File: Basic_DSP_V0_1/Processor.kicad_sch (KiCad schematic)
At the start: 16 parts, among them J12 Conn_ARM_SWD_TagConnect_TC2030, U1 STM32F415RGTx

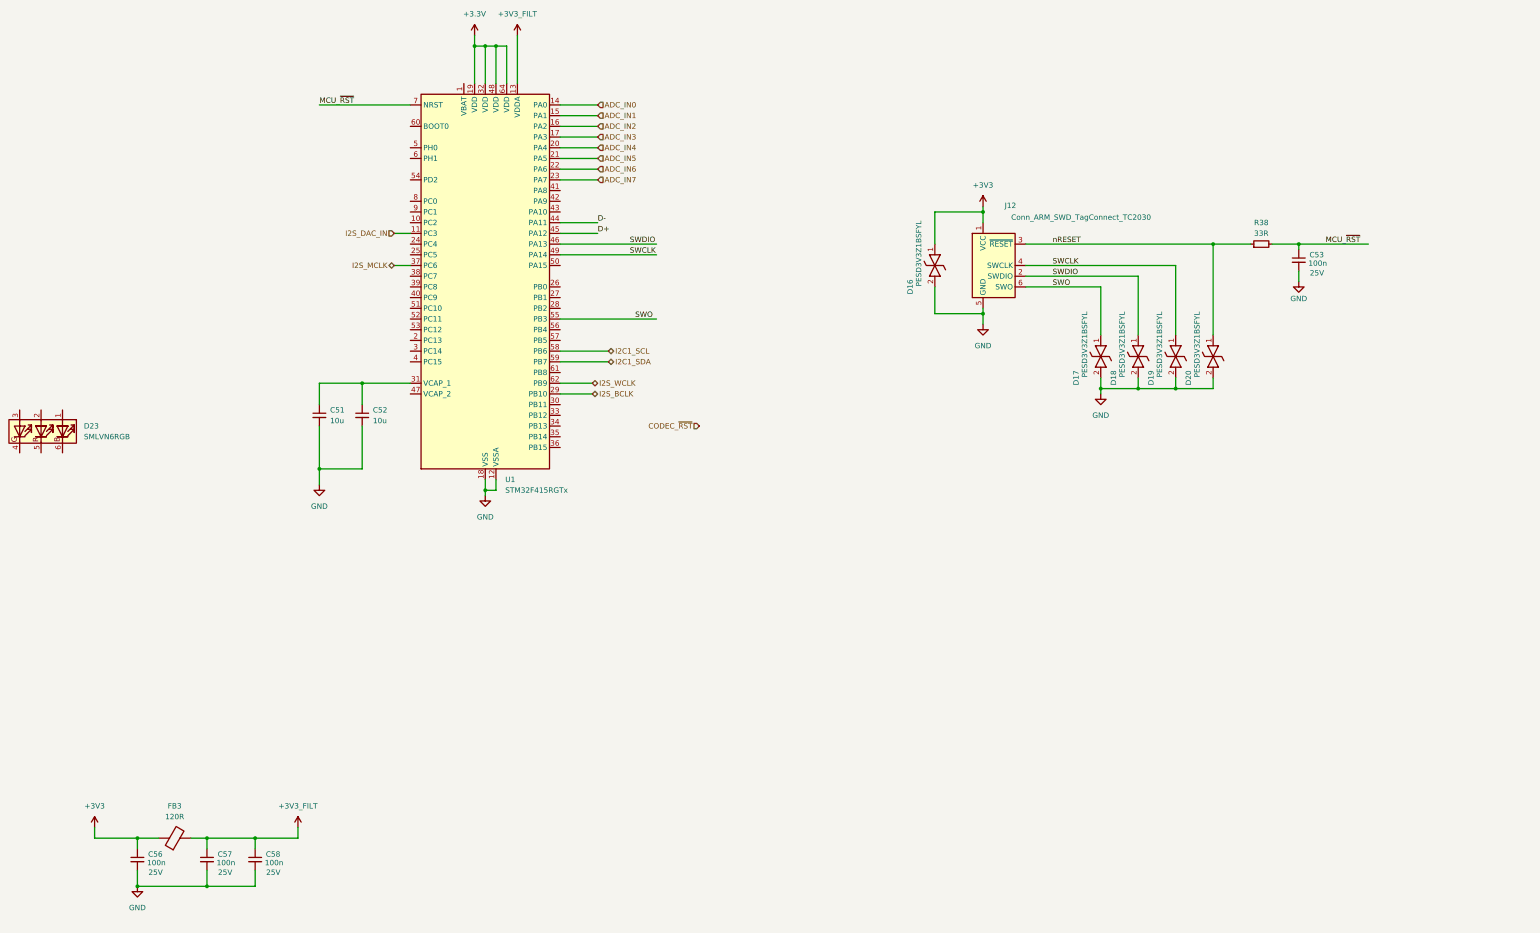
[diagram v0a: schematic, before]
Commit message: Updates to basic DSP schematic
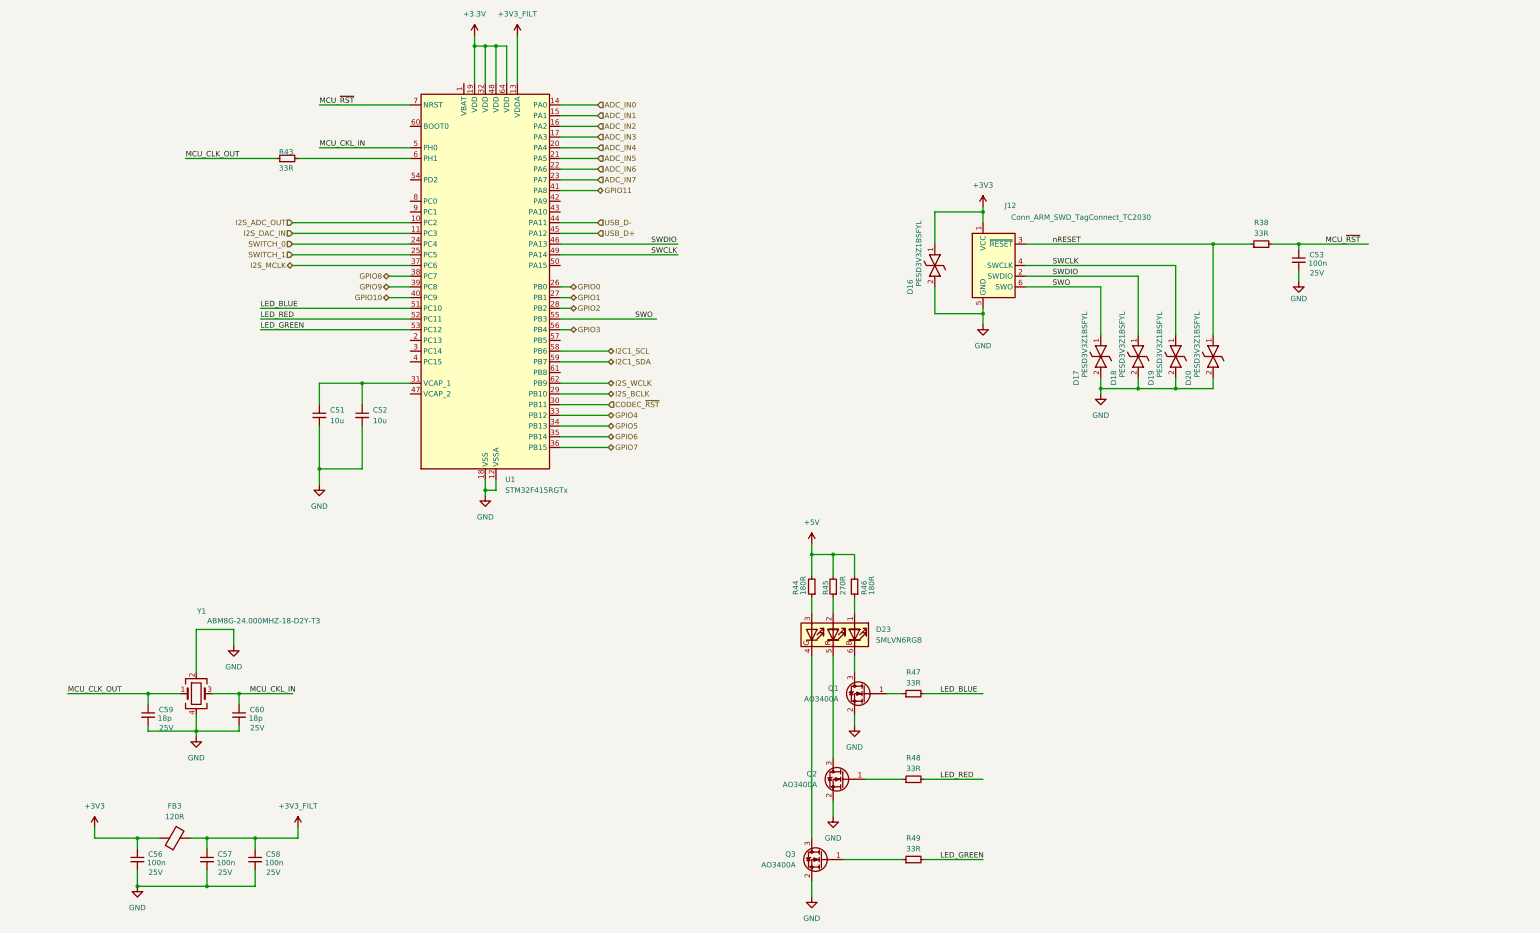
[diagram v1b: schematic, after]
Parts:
- added C59, C60: 18p, Capacitor_SMD:C_0402_1005Metric, symbol Device:C_Small
- added Q1, Q2, Q3: AO3400A, Package_TO_SOT_SMD:SOT-23, symbol Transistor_FET:AO3400A
- added R43, R47, R48, R49: 33R, Resistor_SMD:R_0402_1005Metric_Pad0.72x0.64mm_HandSolder, symbol Device:R_Small
- added R44, R46: 180R, Resistor_SMD:R_0402_1005Metric_Pad0.72x0.64mm_HandSolder, symbol Device:R_Small
- added R45: 270R, Resistor_SMD:R_0402_1005Metric_Pad0.72x0.64mm_HandSolder, symbol Device:R_Small
- added Y1: ABM8G-24.000MHZ-18-D2Y-T3, Crystal:Crystal_SMD_Abracon_ABM8G-4Pin_3.2x2.5mm, symbol Device:Crystal_GND24
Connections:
- net CODEC_~{RST}: now also U1.30 (PB11)
- net GND: now also C59.2, C60.2, Q1.2 (S), Q2.2 (S), Q3.2 (S), Y1.2, Y1.4
- net at D23.1 (BA): now also R46.1
- net at D23.2 (RA): now also R45.1
- net at D23.3 (GA): now also R44.1
- net at D23.4 (GK): now also Q3.3 (D)
- net at D23.5 (RK): now also Q2.3 (D)
- net at D23.6 (BK): now also Q1.3 (D)
- net I2S_ADC_OUT: now reaches U1.10 (PC2)
- net SWITCH_0: now reaches U1.24 (PC4)
- net SWITCH_1: now reaches U1.25 (PC5)
- net GPIO0: now reaches U1.26 (PB0)
- net GPIO1: now reaches U1.27 (PB1)
- net GPIO2: now reaches U1.28 (PB2)
- net GPIO4: now reaches U1.33 (PB12)
- net GPIO5: now reaches U1.34 (PB13)
- net GPIO6: now reaches U1.35 (PB14)
- net GPIO7: now reaches U1.36 (PB15)
- net GPIO8: now reaches U1.38 (PC7)
- net GPIO9: now reaches U1.39 (PC8)
- net GPIO10: now reaches U1.40 (PC9)
- net GPIO11: now reaches U1.41 (PA8)
- net MCU_CKL_IN: now reaches U1.5 (PH0)
- net MCU_CKL_IN: now also C60.1, Y1.3
- net LED_BLUE: now reaches U1.51 (PC10)
- net LED_BLUE: now also R47.2
- net LED_RED: now reaches U1.52 (PC11)
- net LED_RED: now also R48.2
- net LED_GREEN: now reaches U1.53 (PC12)
- net LED_GREEN: now also R49.2
- net GPIO3: now reaches U1.56 (PB4)
- net at U1.6 (PH1): now also R43.2
- net D+ renamed USB_D+
- net D- renamed USB_D-
- new net: Q1.1 (G), R47.1
- new net: Q2.1 (G), R48.1
- new net: Q3.1 (G), R49.1
- new net +5V: R44.2, R45.2, R46.2
- new net MCU_CLK_OUT: C59.1, R43.1, Y1.1
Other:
- moved on the sheet: D23

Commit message: Minor updates to Basic schematic
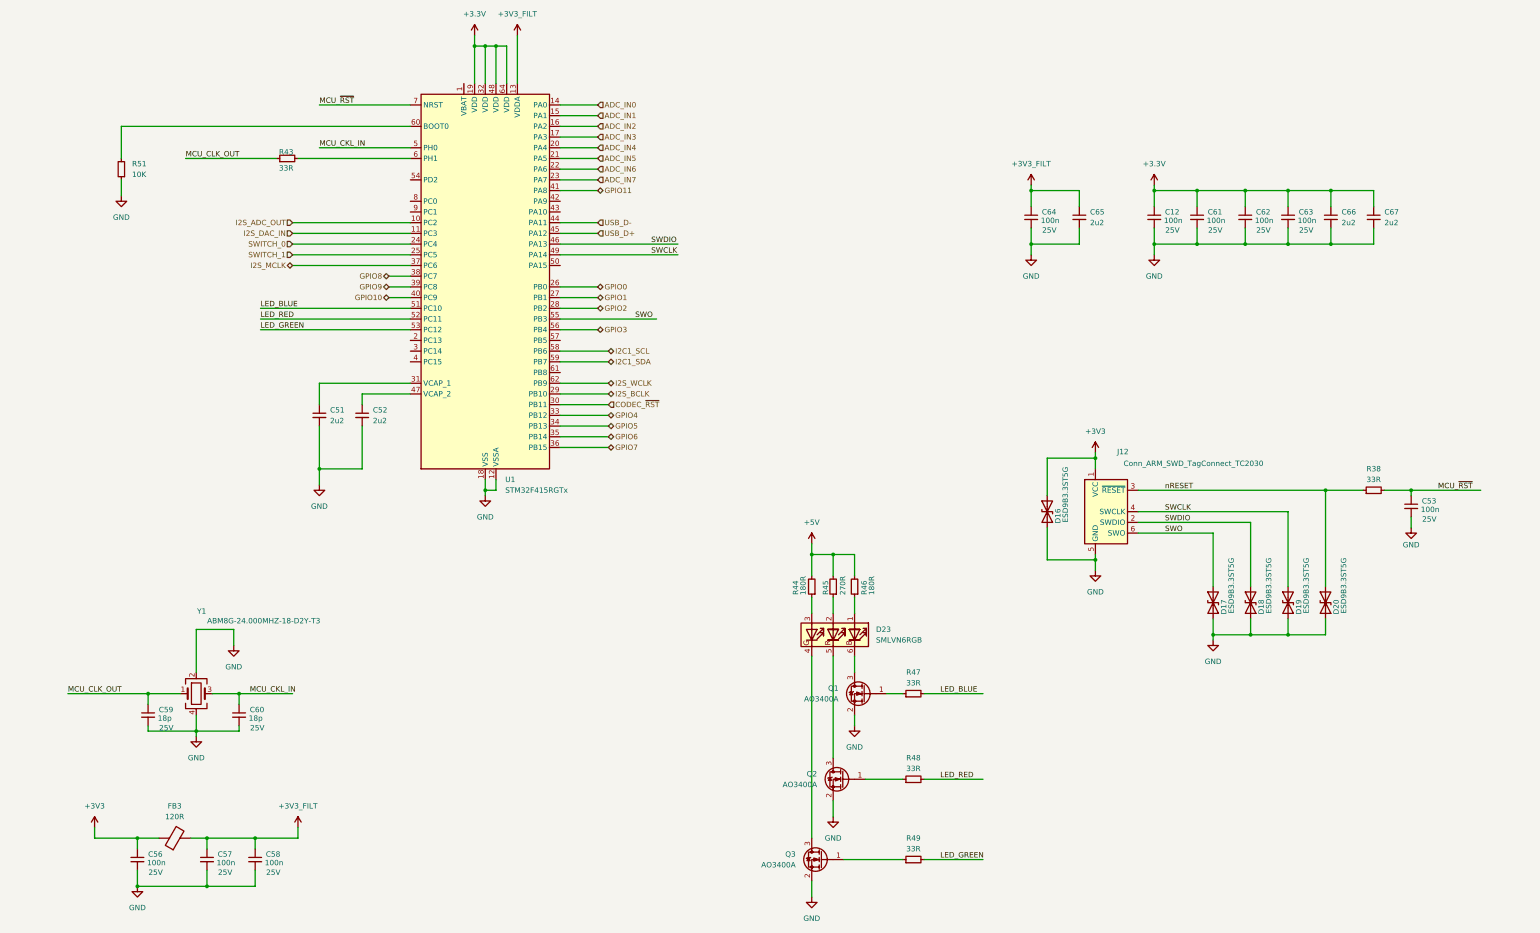
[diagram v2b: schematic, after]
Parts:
- removed D16, D17, D18, D19, D20: PESD3V3Z1BSFYL, symbol Chase_Diode:PESD3V3Z1BSFYL
- added C12: 100n, Capacitor_SMD:C_0603_1608Metric_Pad1.08x0.95mm_HandSolder, symbol Device:C_Small
- added C61, C62, C63, C64: 100n, Capacitor_SMD:C_0402_1005Metric, symbol Device:C_Small
- added C65, C66, C67: 2u2, Capacitor_SMD:C_0805_2012Metric, symbol Device:C_Small
- added D16, D17, D18, D19, D20: ESD9B3.3ST5G, Diode_SMD:D_SOD-923, symbol Diode:ESD9B3.3ST5G
- added R51: 10K, Resistor_SMD:R_0603_1608Metric_Pad0.98x0.95mm_HandSolder, symbol Device:R_Small
- C51, C52: value 10u -> 2u2; MPN CL21B106KOQNNNG -> (none); OC_MOUSER 187-CL21B106KOQNNNG -> (none)
- R38, R43, R44, R45, R46, R47, R48, R49: footprint Resistor_SMD:R_0402_1005Metric_Pad0.72x0.64mm_HandSolder -> Resistor_SMD:R_0603_1608Metric_Pad0.98x0.95mm_HandSolder
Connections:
- net +3.3V: now also C12.1, C61.1, C62.1, C63.1, C66.1, C67.1
- net +3V3: now also D16.2 (A2)
- net +3V3_FILT: now also C64.1, C65.1
- net GND: now also C12.2, C61.2, C62.2, C63.2, C64.2, C65.2, C66.2, C67.2, D16.1 (A1), D17.1 (A1), D18.1 (A1), D19.1 (A1), D20.1 (A1), R51.1
- net SWCLK: now also D19.2 (A2)
- net SWDIO: now also D18.2 (A2)
- net SWO: now also D17.2 (A2)
- net nRESET: now also D20.2 (A2)
- net at C51.1, U1.31 (VCAP_1): no longer C52.1
- net at U1.47 (VCAP_2): now also C52.1
- net at U1.60 (BOOT0): now also R51.2
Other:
- moved on the sheet: C53, J12, R38

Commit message: Started layout
Removed library from repo as it was messin with the links
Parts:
- C53, C56, C57, C58, C59, C60, C61, C62, C63, C64: footprint Capacitor_SMD:C_0402_1005Metric -> Capacitor_SMD:C_0603_1608Metric_Pad1.08x0.95mm_HandSolder
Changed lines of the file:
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@@
 			)
 		)
-		(property "Footprint" "Capacitor_SMD:C_0402_1005Metric"
+		(property "Footprint" "Capacitor_SMD:C_0603_1608Metric_Pad1.08x0.95mm_HandSolder"
 			(at 87.63 191.77 0)
 			(effects
@@
 			)
 		)
-		(property "Footprint" "Capacitor_SMD:C_0402_1005Metric"
+		(property "Footprint" "Capacitor_SMD:C_0603_1608Metric_Pad1.08x0.95mm_HandSolder"
 			(at 91.44 226.06 0)
 			(effects
@@
 			)
 		)
-		(property "Footprint" "Capacitor_SMD:C_0402_1005Metric"
+		(property "Footprint" "Capacitor_SMD:C_0603_1608Metric_Pad1.08x0.95mm_HandSolder"
 			(at 80.01 226.06 0)
 			(effects
@@
 			)
 		)
-		(property "Footprint" "Capacitor_SMD:C_0402_1005Metric"
+		(property "Footprint" "Capacitor_SMD:C_0603_1608Metric_Pad1.08x0.95mm_HandSolder"
 			(at 365.76 142.24 0)
 			(effects
@@
 			)
 		)
-		(property "Footprint" "Capacitor_SMD:C_0402_1005Metric"
+		(property "Footprint" "Capacitor_SMD:C_0603_1608Metric_Pad1.08x0.95mm_HandSolder"
 			(at 275.59 73.66 0)
 			(effects
@@
 			)
 		)
-		(property "Footprint" "Capacitor_SMD:C_0402_1005Metric"
+		(property "Footprint" "Capacitor_SMD:C_0603_1608Metric_Pad1.08x0.95mm_HandSolder"
 			(at 326.39 73.66 0)
 			(effects
@@
 			)
 		)
-		(property "Footprint" "Capacitor_SMD:C_0402_1005Metric"
+		(property "Footprint" "Capacitor_SMD:C_0603_1608Metric_Pad1.08x0.95mm_HandSolder"
 			(at 66.04 191.77 0)
 			(effects
@@
 			)
 		)
-		(property "Footprint" "Capacitor_SMD:C_0402_1005Metric"
+		(property "Footprint" "Capacitor_SMD:C_0603_1608Metric_Pad1.08x0.95mm_HandSolder"
 			(at 336.55 73.66 0)
 			(effects
@@
 			)
 		)
-		(property "Footprint" "Capacitor_SMD:C_0402_1005Metric"
+		(property "Footprint" "Capacitor_SMD:C_0603_1608Metric_Pad1.08x0.95mm_HandSolder"
 			(at 63.5 226.06 0)
 			(effects
@@
 			)
 		)
-		(property "Footprint" "Capacitor_SMD:C_0402_1005Metric"
+		(property "Footprint" "Capacitor_SMD:C_0603_1608Metric_Pad1.08x0.95mm_HandSolder"
 			(at 314.96 73.66 0)
 			(effects

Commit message: Basic placement on PCB
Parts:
- added C75, C76: 2u2, Capacitor_SMD:C_0805_2012Metric, symbol Device:C_Small
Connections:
- net +3.3V: now also C75.1, C76.1
- net GND: now also C75.2, C76.2

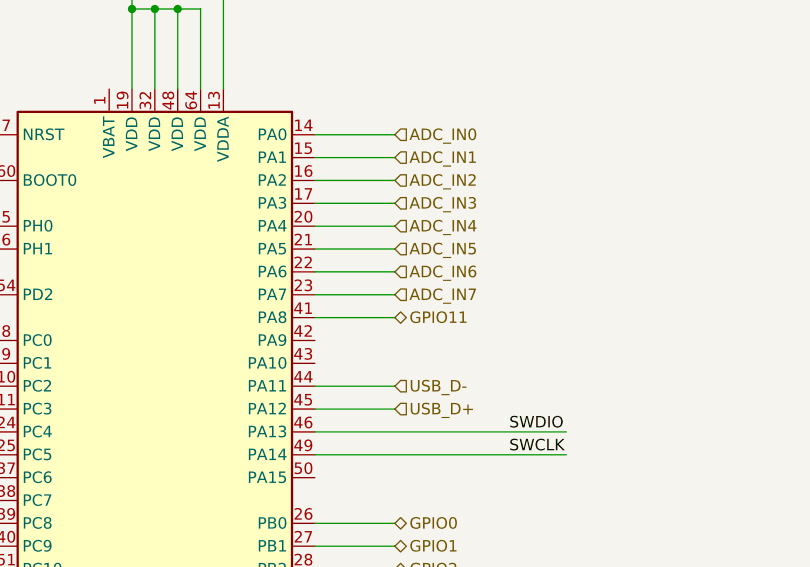
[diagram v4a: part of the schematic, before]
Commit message: Updated parts with LCSC order codes
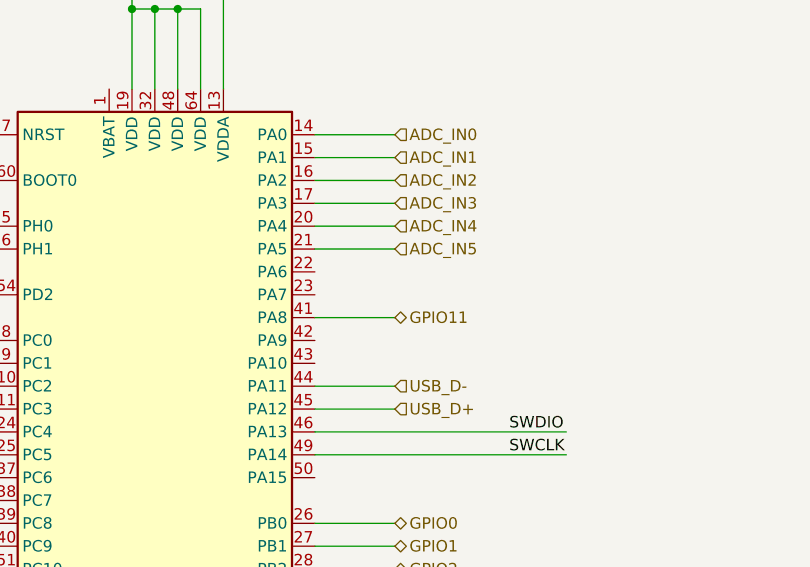
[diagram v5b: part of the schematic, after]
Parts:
- C12, C53, C56, C57, C58, C61, C62, C63, C64: MF TAIYO YUDEN -> FH (Guangdong Fenghua Advanced Tech); MPN MBAST105SB7104KFNA01 -> 0603B104M250NT; OC_LCSC (none) -> C336628
- C51, C52, C65, C66, C67, C75, C76: footprint Capacitor_SMD:C_0805_2012Metric -> Capacitor_SMD:C_0603_1608Metric_Pad1.08x0.95mm_HandSolder; MF Samsung Electro-Mechanics -> FH (Guangdong Fenghua Advanced Tech); MPN (none) -> 0603B225K250NT; OC_LCSC (none) -> C99228; Voltage (none) -> 25V
- C59, C60: MF TAIYO YUDEN -> Walsin Tech Corp; MPN MBAST105SB7104KFNA01 -> RF18N180F500CT; OC_LCSC (none) -> C2909435
- D16, D17, D18, D19, D20: MF (none) -> TECH PUBLIC; MPN (none) -> ESD9B3.3ST5G; OC_LCSC (none) -> C3040608
- D23: MF (none) -> ROHM Semicon; MPN (none) -> SMLVN6RGB1W1; OC_LCSC (none) -> C2842809
- FB3: OC_LCSC (none) -> C85831
- Q1, Q2, Q3: MF (none) -> Alpha & Omega Semicon; MPN (none) -> AO3400A; OC_LCSC (none) -> C20917
- R38, R43, R47, R48, R49: MF (none) -> Walsin Tech Corp; MPN (none) -> WR06X33R0FTL; OC_LCSC (none) -> C163909
- R44, R46: MF (none) -> UNI-ROYAL(Uniroyal Elec); MPN (none) -> 0603WAF1800T5E; OC_LCSC (none) -> C22828
- R45: MF (none) -> UNI-ROYAL(Uniroyal Elec); MPN (none) -> 0603WAF2700T5E; OC_LCSC (none) -> C22966
- R51: MF (none) -> UNI-ROYAL(Uniroyal Elec); MPN (none) -> 0603WAF1002T5E; OC_LCSC (none) -> C25804
- U1: MF (none) -> STMicroelectronics; MPN (none) -> STM32F415RGT6; OC_LCSC (none) -> C124726
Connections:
- net ADC_IN6: no longer names the net of U1.22 (PA6)
- net ADC_IN7: no longer names the net of U1.23 (PA7)

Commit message: WIP - small layout progress on basic DSP
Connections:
- net +3.3V is gone; now on net +3V3: C12.1, C61.1, C62.1, C63.1, C66.1, C67.1, C75.1, C76.1, U1.19 (VDD), U1.32 (VDD), U1.48 (VDD), U1.64 (VDD)
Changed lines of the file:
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@@
 			)
 		)
-		(property "Value" "+3.3V"
+		(property "Value" "+3V3"
 			(at 143.51 25.4 0)
 			(effects
@@
 			)
 		)
-		(property "Value" "+3.3V"
+		(property "Value" "+3V3"
 			(at 304.8 60.96 0)
 			(effects
